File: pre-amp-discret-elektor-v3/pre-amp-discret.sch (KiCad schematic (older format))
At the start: 64 parts, among them J1 Conn_01x01, J2 Conn_01x01, J3 Conn_01x01, J4 Conn_01x01, J5 Conn_01x01, J6 Conn_01x01, J7 Conn_01x01, Q1 BCM857DS,115, Q11 BCM847DS,115, Q13 BCM847DS,115, Q2 BC850C, Q3 BCM857DS,115, Q4 BC550C, Q5 BC560C, Q6 BC337-40, Q7 BC860C, Q8 BC327-40

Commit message: V3 Layout completed
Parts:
- removed Q1: BCM857DS,115, Package_SO:SC-74-6_1.5x2.9mm_P0.95mm, symbol kicad-snk:BCM857DS,115
- removed Q13: BCM847DS,115, Package_SO:SC-74-6_1.5x2.9mm_P0.95mm, symbol kicad-snk:BCM847DS,115
- added Q1: THAT340, Package_SO:SOIC-14_3.9x8.7mm_P1.27mm, symbol kicad-snk:THAT340
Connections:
- net at R6.1: now also Q1.8 (E)
- net at Q2.1 (B), R3.1: now also Q1.7 (E)
- net at C21.2, R1.1, R32.1: now also Q1.2 (B), Q1.6 (B)
- net at C12.2, R8.1, R9.2: now also Q1.13 (B), Q1.9 (B)
- net at R2.2: now also Q1.5 (C)
- net at R5.2: now also Q1.10
- net at Q7.1 (B), R20.2: now also Q1.1 (C)
- net at R21.1: now also Q1.3 (E)
- net at R23.2: now also Q1.14 (C)
- net at R24.1: now also Q1.12 (E)
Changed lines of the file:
@@
 Title "Discrete Pre-Amp Elektor"
 Date "2021-02-10"
-Rev "V2"
+Rev "V3"
 Comp ""
 Comment1 ""
@@
 $EndComp
 $Comp
-L kicad-snk:BCM847DS,115 Q13
-U 1 1 5FF125E4
-P 3100 3800
-F 0 "Q13" H 3290 3846 50  0000 L CNN
-F 1 "BCM847DS,115" H 3290 3755 50  0000 L CNN
-F 2 "Package_SO:SC-74-6_1.5x2.9mm_P0.95mm" H 3100 3800 50  0001 C CNN
-F 3 "https://www.analog.com/media/en/technical-documentation/obsolete-data-sheets/SSM2210.pdf" H 3100 3800 50  0001 C CNN
-	1    3100 3800
-	1    0    0    -1
-$EndComp
-$Comp
-L kicad-snk:BCM847DS,115 Q13
-U 2 1 5FF14014
-P 4100 3800
-F 0 "Q13" H 4291 3846 50  0000 L CNN
-F 1 "BCM847DS,115" H 4291 3755 50  0000 L CNN
-F 2 "Package_SO:SC-74-6_1.5x2.9mm_P0.95mm" H 4100 3800 50  0001 C CNN
-F 3 "https://www.analog.com/media/en/technical-documentation/obsolete-data-sheets/SSM2210.pdf" H 4100 3800 50  0001 C CNN
-	2    4100 3800
-	-1   0    0    -1
-$EndComp
-$Comp
 L kicad-snk:BCM857DS,115 Q3
 U 2 1 5FF89211
@@
 	-1   0    0    1
 $EndComp
-$Comp
-L kicad-snk:BCM857DS,115 Q1
-U 1 1 6002025B
-P 5400 5150
-F 0 "Q1" H 5590 5104 50  0000 L CNN
-F 1 "BCM857DS,115" H 5590 5195 50  0000 L CNN
-F 2 "Package_SO:SC-74-6_1.5x2.9mm_P0.95mm" H 5400 5150 50  0001 C CNN
-F 3 "https://www.analog.com/media/en/technical-documentation/data-sheets/SSM2220.pdf" H 5400 5150 50  0001 C CNN
-	1    5400 5150
-	1    0    0    1
-$EndComp
-$Comp
-L kicad-snk:BCM857DS,115 Q1
-U 2 1 60023185
-P 6400 5150
-F 0 "Q1" H 6591 5104 50  0000 L CNN
-F 1 "BCM857DS,115" H 6591 5195 50  0000 L CNN
-F 2 "Package_SO:SC-74-6_1.5x2.9mm_P0.95mm" H 6400 5150 50  0001 C CNN
-F 3 "https://www.analog.com/media/en/technical-documentation/data-sheets/SSM2220.pdf" H 6400 5150 50  0001 C CNN
-	2    6400 5150
-	-1   0    0    1
-$EndComp
 Wire Wire Line
 	3200 1200 4000 1200
@@
 Wire Wire Line
 	4300 3800 6800 3800
+$Comp
+L kicad-snk:THAT340 Q1
+U 3 1 60284C07
+P 5400 5150
+F 0 "Q1" H 5590 5196 50  0000 L CNN
+F 1 "THAT340" H 5590 5105 50  0000 L CNN
+F 2 "" H 5590 5059 50  0000 L CNN
+F 3 "" H 5590 5059 50  0000 L CNN
+	3    5400 5150
+	1    0    0    -1
+$EndComp
+$Comp
+L kicad-snk:THAT340 Q1
+U 4 1 60285CA6
+P 6400 5150
+F 0 "Q1" H 6590 5196 50  0000 L CNN
+F 1 "THAT340" H 6590 5105 50  0000 L CNN
+F 2 "" H 6589 5059 50  0000 L CNN
+F 3 "" H 6590 5059 50  0000 L CNN
+	4    6400 5150
+	-1   0    0    -1
+$EndComp
+$Comp
+L kicad-snk:THAT340 Q1
+U 1 1 6024A272
+P 3100 3800
+F 0 "Q1" H 3290 3891 50  0000 L CNN
+F 1 "THAT340" H 3290 3800 50  0000 L CNN
+F 2 "Package_SO:SOIC-14_3.9x8.7mm_P1.27mm" H 3290 3709 50  0000 L CNN
+F 3 "" H 3290 3709 50  0000 L CNN
+	1    3100 3800
+	1    0    0    -1
+$EndComp
+$Comp
+L kicad-snk:THAT340 Q1
+U 2 1 6024A424
+P 4100 3800
+F 0 "Q1" H 4289 3891 50  0000 L CNN
+F 1 "THAT340" H 4289 3800 50  0000 L CNN
+F 2 "Package_SO:SOIC-14_3.9x8.7mm_P1.27mm" H 4289 3709 50  0000 L CNN
+F 3 "" H 4290 3709 50  0000 L CNN
+	2    4100 3800
+	-1   0    0    -1
+$EndComp
 $EndSCHEMATC

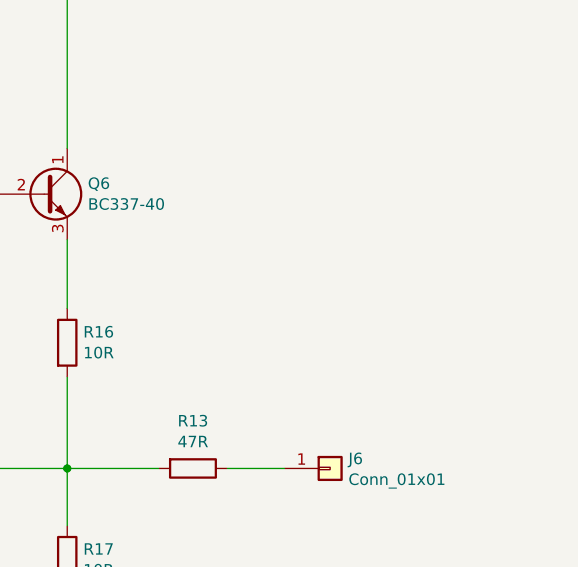
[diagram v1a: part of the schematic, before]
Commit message: Adding note for idle current
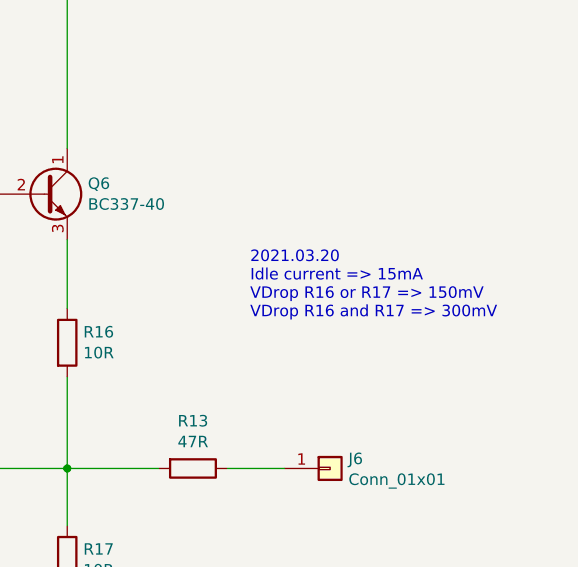
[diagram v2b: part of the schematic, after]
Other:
- note added: "2021.03.20\nIdle current => 15mA\nVDrop R16 or R17 => 150mV\nVDrop R16 and R17 => 300mV"
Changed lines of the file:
@@
 	-1   0    0    -1
 $EndComp
+Text Notes 13550 3800 0    50   ~ 0
+2021.03.20\nIdle current => 15mA\nVDrop R16 or R17 => 150mV\nVDrop R16 and R17 => 300mV
 $EndSCHEMATC
